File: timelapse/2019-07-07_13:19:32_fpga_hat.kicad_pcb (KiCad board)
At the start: 4 copper layers, 65 x 56.5 mm, 92 parts, among them J1 2x20, J2 AudioJack3, J3 Conn_02x06_Top_Bottom, J4 Conn_02x06_Top_Bottom, J5 Conn_02x06_Top_Bottom, J6 Conn_01x02, SW1 PTS815, SW2 PTS815, SW3 PTS815, SW4 PTS815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

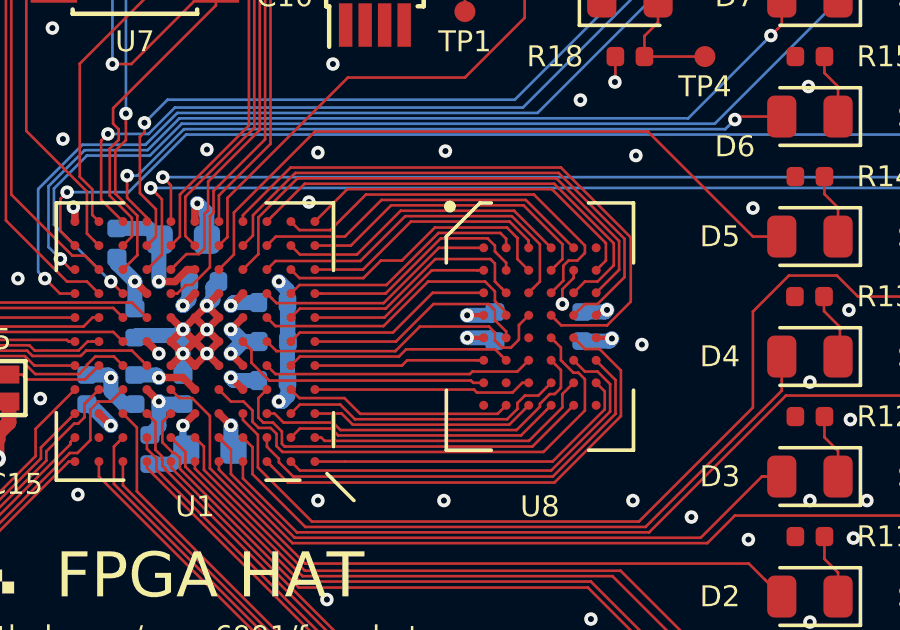
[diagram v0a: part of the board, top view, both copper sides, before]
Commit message: Tidy up SRAM escape and decoupling
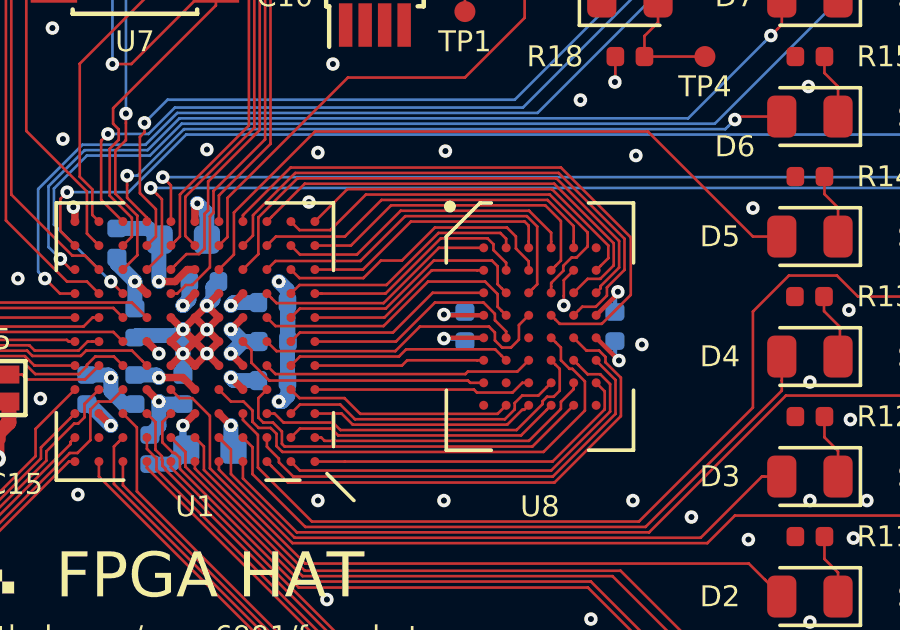
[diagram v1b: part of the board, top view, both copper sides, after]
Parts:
- moved C27 1.10 mm to (146.5, 106.0)
- moved C26 1.00 mm to (141.5, 106.0)
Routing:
- net +3V3: track 45.8 -> 46.8 mm
- net GND: track 32.2 -> 33.0 mm
